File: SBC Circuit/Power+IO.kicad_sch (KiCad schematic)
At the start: 16 parts, among them J1 USB_B, Q1 AOI21357, Q2 AOI21357, SW2 SW_DIP_x08, U10 LD1117AV33, U8 FT230XS, U9 LM7805_TO220

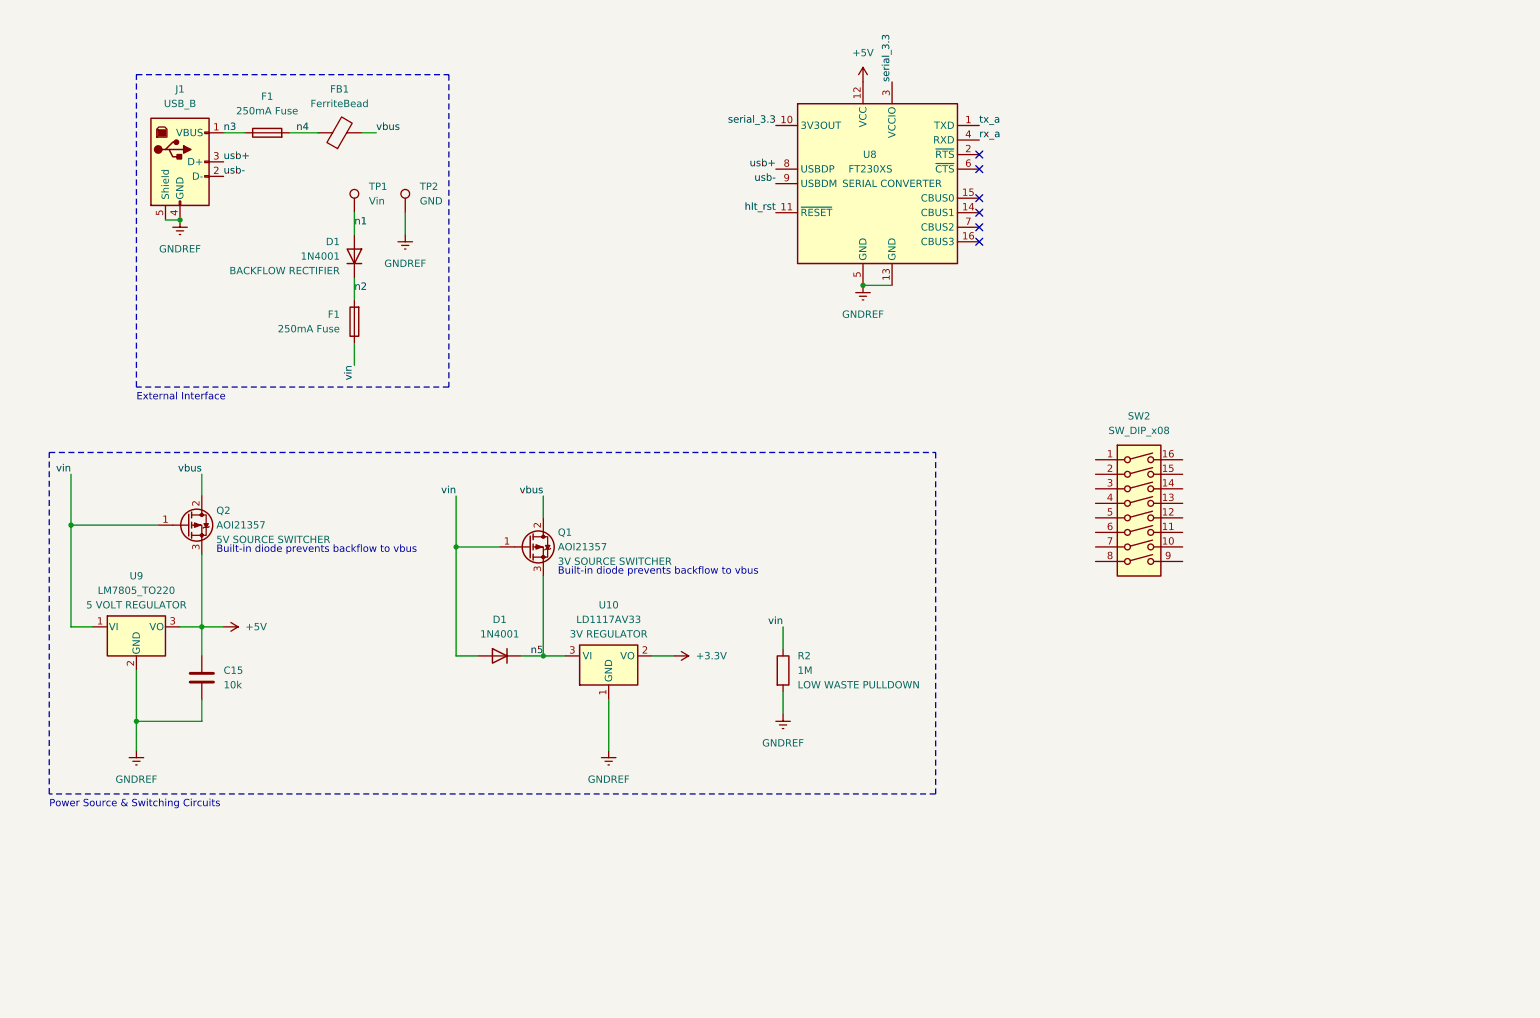
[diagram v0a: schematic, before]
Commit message: Updates to Schematic
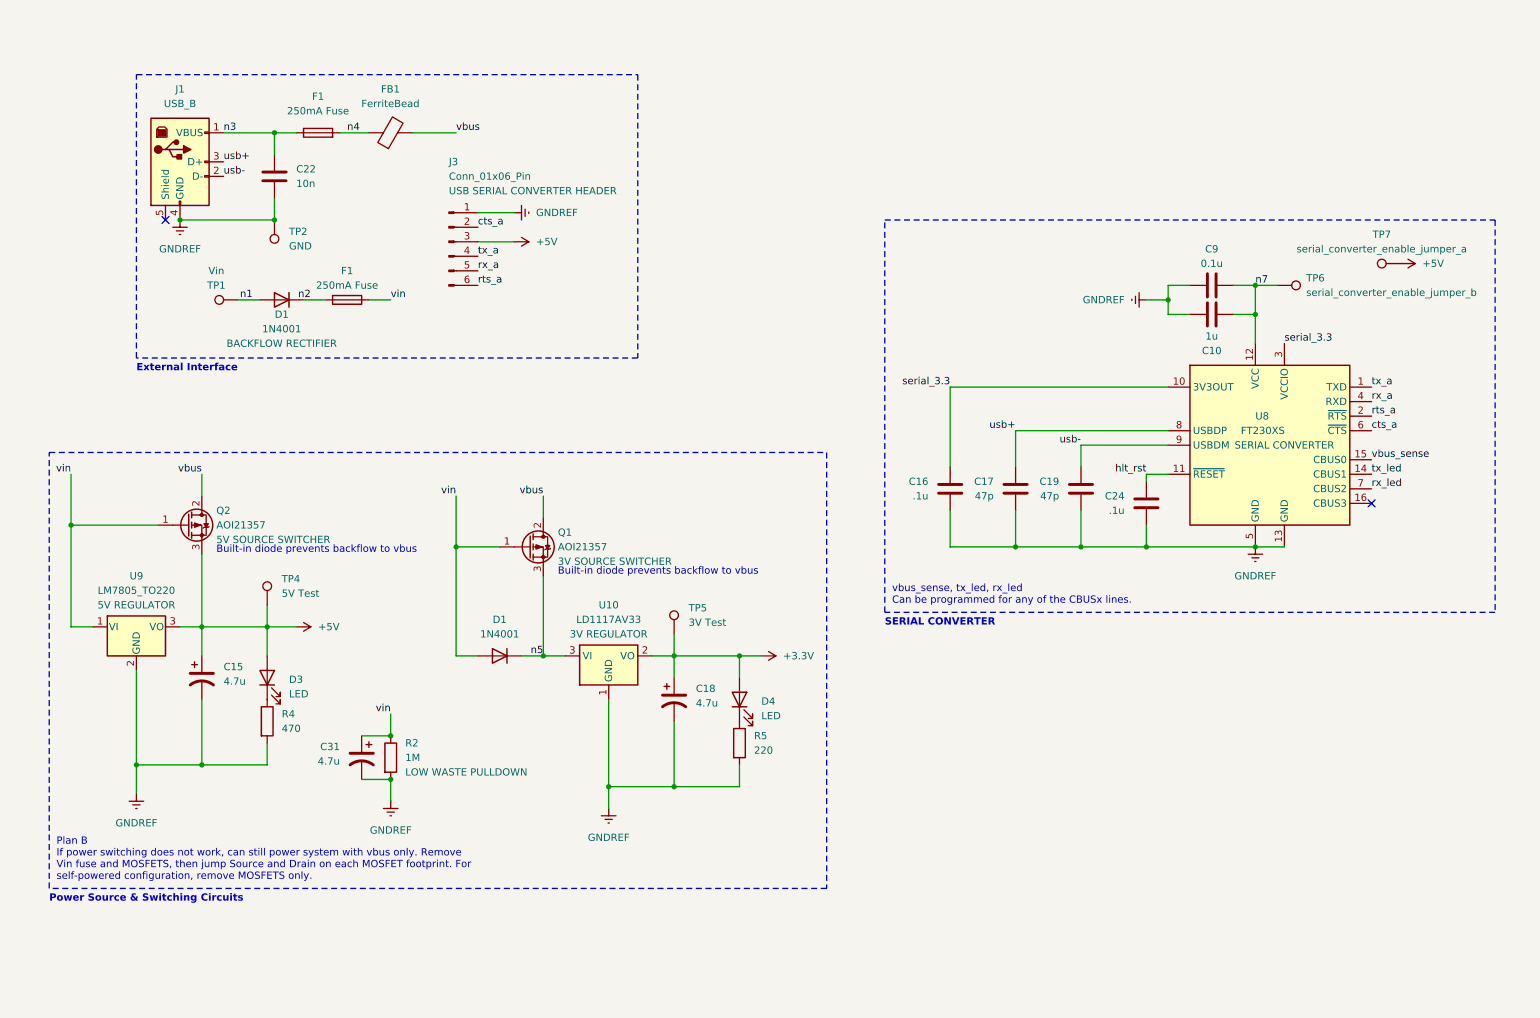
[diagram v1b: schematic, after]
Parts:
- removed C15: 10k, symbol Device:C
- removed SW2: SW_DIP_x08, symbol Switch:SW_DIP_x08
- added C10: 1u, symbol Device:C
- added C15, C18, C31: 4.7u, symbol Device:C_Polarized_US
- added C16, C24: .1u, symbol Device:C
- added C17, C19: 47p, symbol Device:C
- added C22: 10n, symbol Device:C
- added C9: 0.1u, symbol Device:C
- added D3, D4: LED, symbol Device:LED
- added J3: Conn_01x06_Pin, symbol Connector:Conn_01x06_Pin
- added R4: 470, symbol Device:R
- added R5: 220, symbol Device:R
- added TP4: 5V Test, symbol Connector:TestPoint
- added TP5: 3V Test, symbol Connector:TestPoint
- added TP6: serial_converter_enable_jumper_b, symbol Connector:TestPoint
- added TP7: serial_converter_enable_jumper_a, symbol Connector:TestPoint
- U9: Role 5 VOLT REGULATOR -> 5V REGULATOR
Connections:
- net +3.3V: now also C18.1, D4.2 (A), TP5.1
- net +5V: now also C15.1, D3.2 (A), J3.3 (Pin_3), TP4.1, TP7.1; no longer U8.12 (VCC)
- net GNDREF: now also C10.2, C15.2, C16.1, C17.1, C18.2, C19.2, C22.2, C24.1, C31.2, C9.2, J3.1 (Pin_1), R4.2, R5.2; no longer J1.5 (Shield)
- net hlt_rst: now also C24.2
- net n3: now also C22.1
- net rx_a: now also J3.5 (Pin_5)
- net serial_3.3: now also C16.2
- net tx_a: now also J3.4 (Pin_4)
- net usb+: now also C17.2
- net usb-: now also C19.1
- net vin: now also C31.1
- net tx_led: now reaches U8.14 (CBUS1)
- net vbus_sense: now reaches U8.15 (CBUS0)
- net rts_a: now reaches U8.2 (~{RTS})
- net rts_a: now also J3.6 (Pin_6)
- net cts_a: now reaches U8.6 (~{CTS})
- net cts_a: now also J3.2 (Pin_2)
- net rx_led: now reaches U8.7 (CBUS2)
- new net: D4.1 (K), R5.1
- new net: D3.1 (K), R4.1
- new net n7: C10.1, C9.1, TP6.1, U8.12 (VCC)
- no-connect marks 6 -> 2
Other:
- note added: "Plan B If power switching does not work, can still power system with vbus only. Remove Vin fuse and MOSFETS, then jump Source and Drain on each MOSFET footprint. For self-powered configuration, remove MOSFETS only."
- note added: "SERIAL CONVERTER"
- note added: "vbus_sense, tx_led, rx_led Can be programmed for any of the CBUSx lines."
- moved on the sheet: D1, F1, FB1, R2, TP1, TP2, U8

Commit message: Small changes to prepare for review
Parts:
- added D5, D6: LED, symbol Device:LED
- added R10, R9: 220, symbol Device:R
- added R7, R8: R, symbol Device:R
- renumbered C9 to C25, C10 to C26, D1 to D2, F1 to F2, Q2 to Q1, Q1 to Q2, U8 to U10, U9 to U8, U10 to U9
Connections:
- net GNDREF: now also R8.2
- net rx_led: now also R10.2
- net serial_3.3: now also D5.2 (A), D6.2 (A)
- net tx_led: now also R9.2
- net vbus: now also R7.1
- net vbus_sense: no longer names the net of U10.15 (CBUS0)
- net vbus_sense: now also R7.2, R8.1
- new net: D5.1 (K), R9.1
- new net: D6.1 (K), R10.1
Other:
- moved on the sheet: C15, C16, C17, C18, C19, C22, C24, C25, C26, C31, D1, D2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

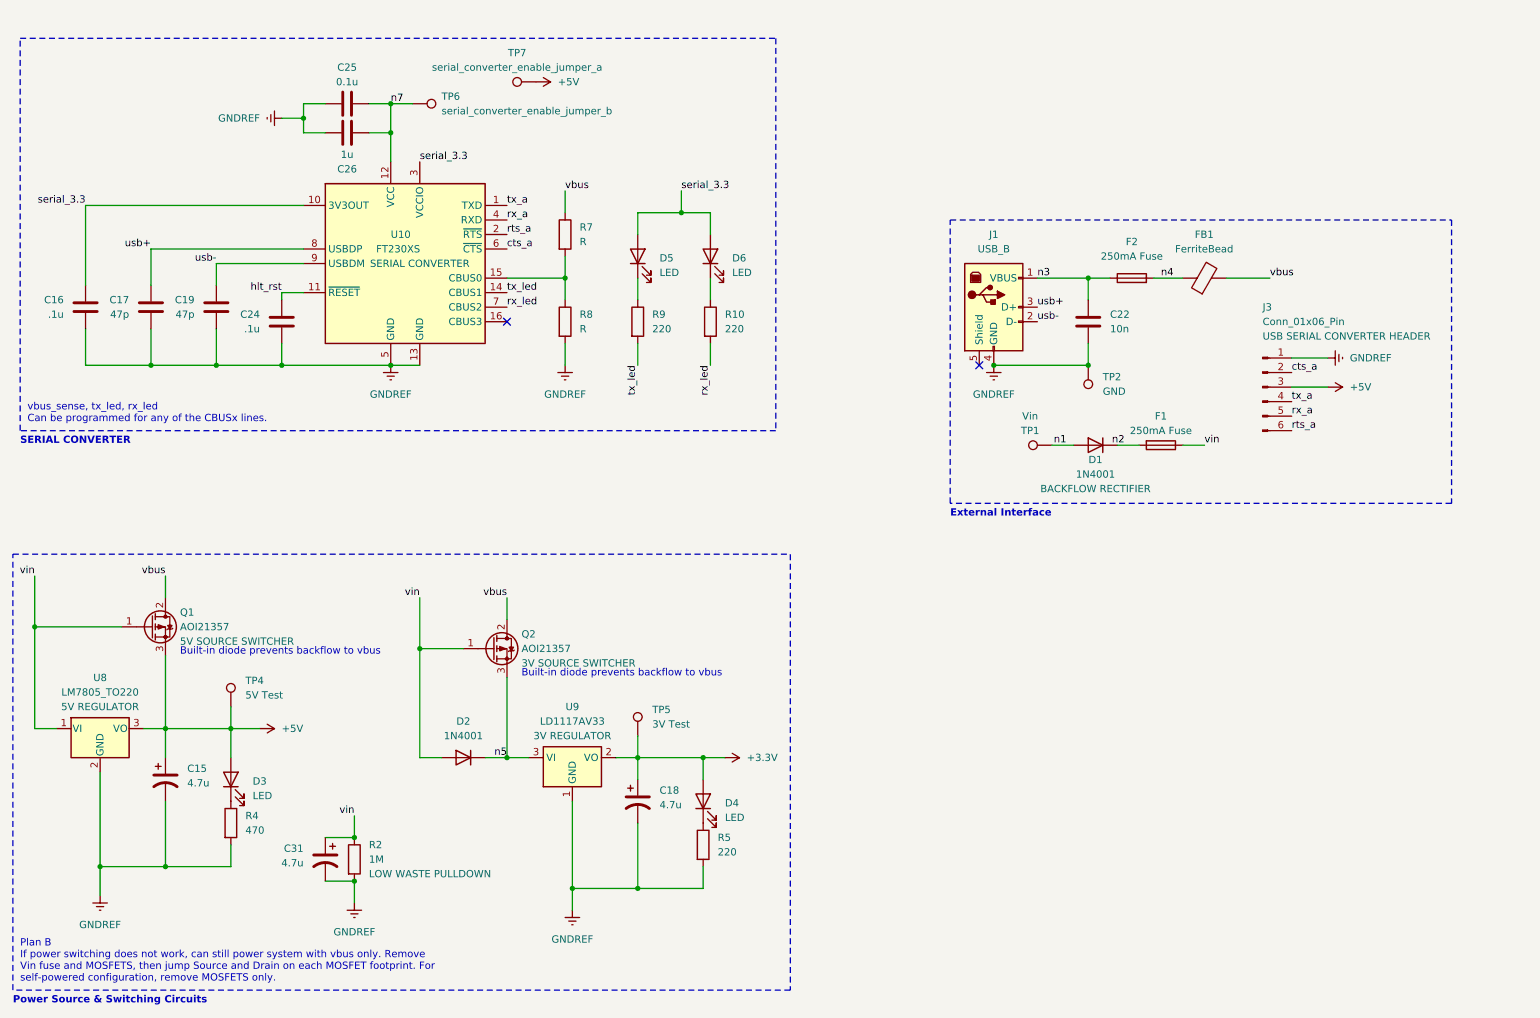
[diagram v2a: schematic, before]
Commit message: New part selections, serial port selection
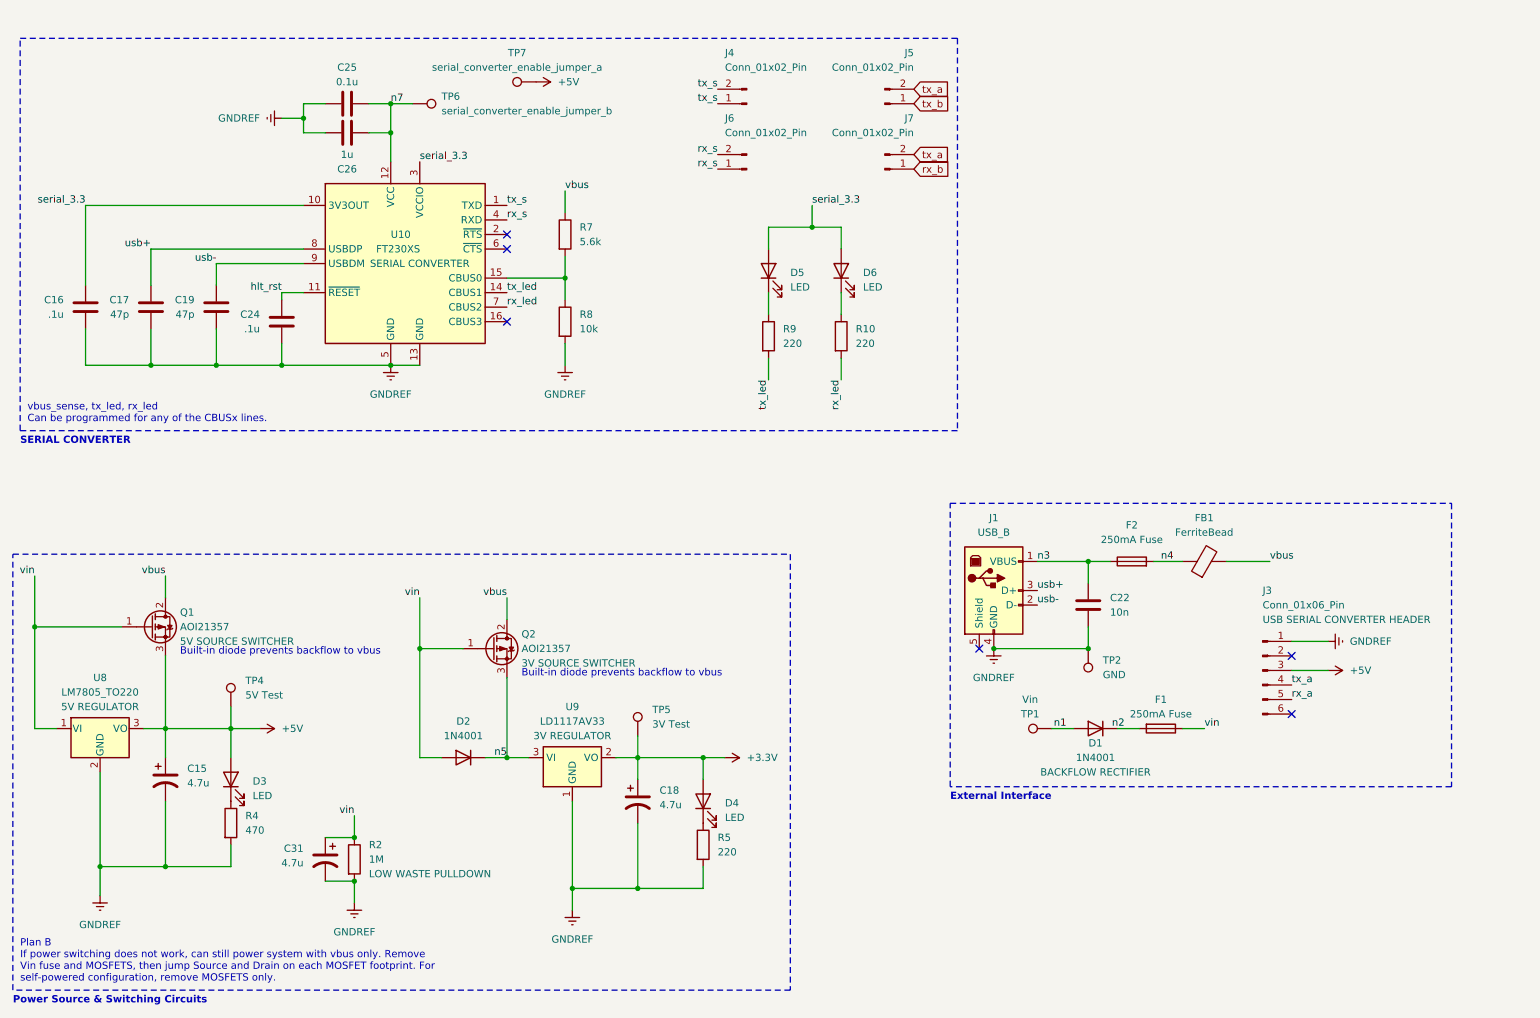
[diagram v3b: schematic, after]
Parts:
- added J4, J5, J6, J7: Conn_01x02_Pin, symbol Connector:Conn_01x02_Pin
- R7: value R -> 5.6k
- R8: value R -> 10k
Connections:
- net rx_a: no longer U10.4 (RXD)
- net tx_a: now also J5.2 (Pin_2), J7.2 (Pin_2); no longer U10.1 (TXD)
- net cts_a: no longer names the net of J3.2 (Pin_2)
- net cts_a: no longer U10.6 (~{CTS})
- net rts_a: no longer names the net of J3.6 (Pin_6)
- net rts_a: no longer U10.2 (~{RTS})
- new net rx_b: J7.1 (Pin_1)
- new net rx_s: J6.1 (Pin_1), J6.2 (Pin_2), U10.4 (RXD)
- new net tx_b: J5.1 (Pin_1)
- new net tx_s: J4.1 (Pin_1), J4.2 (Pin_2), U10.1 (TXD)
- no-connect marks 2 -> 6
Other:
- moved on the sheet: C22, D1, D5, D6, F1, F2, FB1, J1, J3, R10, R9, TP1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
